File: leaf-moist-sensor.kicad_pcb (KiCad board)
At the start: 2 copper layers, 61 x 61 mm, 2 parts, among them P1 CONN_01X02

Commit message: 1mm Clearance + gerbers
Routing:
- net /SENSOR_TRACK: track 733.1 -> 690.1 mm
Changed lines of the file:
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@@
   )
   (setup
-    (last_trace_width 0.7)
+    (last_trace_width 0.25)
     (user_trace_width 0.7)
     (trace_clearance 0.2)
-    (zone_clearance 0.508)
+    (zone_clearance 1)
     (zone_45_only no)
     (trace_min 0.2)
@@
       (drillshape 0)
       (scaleselection 1)
-      (outputdirectory "05mmGerbers"))
+      (outputdirectory "1mmGerbers"))
   )
   (net 0 "")
@@
   (segment (start 132.85 60.1) (end 132.55 60.4) (width 0.7) (layer F.Cu) (net 1))
   (segment (start 132.85 57.85) (end 132.85 60.1) (width 0.7) (layer F.Cu) (net 1))
-  (segment (start 134.05 62.5) (end 134.05 114.6) (width 0.7) (layer F.Cu) (net 2))
-  (segment (start 134.1 62.8) (end 149.323337 62.8) (width 0.7) (layer F.Cu) (net 2))
-  (segment (start 134.1 66.3) (end 153.695918 66.3) (width 0.7) (layer F.Cu) (net 2))
-  (segment (start 134.1 69.8) (end 156.721892 69.8) (width 0.7) (layer F.Cu) (net 2))
-  (segment (start 134.1 73.3) (end 158.899194 73.3) (width 0.7) (layer F.Cu) (net 2))
-  (segment (start 134.1 76.8) (end 160.439134 76.8) (width 0.7) (layer F.Cu) (net 2))
-  (segment (start 134.1 80.3) (end 161.449589 80.3) (width 0.7) (layer F.Cu) (net 2))
-  (segment (start 134.1 83.8) (end 161.98817 83.8) (width 0.7) (layer F.Cu) (net 2))
-  (segment (start 134.1 87.3) (end 162.082137 87.3) (width 0.7) (layer F.Cu) (net 2))
-  (segment (start 134.1 90.8) (end 161.736027 90.8) (width 0.7) (layer F.Cu) (net 2))
-  (segment (start 134.1 94.3) (end 160.932816 94.3) (width 0.7) (layer F.Cu) (net 2))
-  (segment (start 134.1 97.8) (end 159.629395 97.8) (width 0.7) (layer F.Cu) (net 2))
-  (segment (start 134.1 101.3) (end 157.743181 101.3) (width 0.7) (layer F.Cu) (net 2))
-  (segment (start 134.1 104.8) (end 155.11785 104.8) (width 0.7) (layer F.Cu) (net 2))
-  (segment (start 134.1 108.3) (end 151.420508 108.3) (width 0.7) (layer F.Cu) (net 2))
-  (segment (start 134.1 111.8) (end 145.665034 111.8) (width 0.7) (layer F.Cu) (net 2))
-  (segment (start 134.05 64.55) (end 116.41658 64.55) (width 0.7) (layer F.Cu) (net 2))
-  (segment (start 134.05 68.05) (end 112.814711 68.05) (width 0.7) (layer F.Cu) (net 2))
-  (segment (start 134.05 71.55) (end 110.250053 71.55) (width 0.7) (layer F.Cu) (net 2))
-  (segment (start 134.05 75.05) (end 108.409456 75.05) (width 0.7) (layer F.Cu) (net 2))
-  (segment (start 134.05 78.55) (end 107.143913 78.55) (width 0.7) (layer F.Cu) (net 2))
-  (segment (start 134.05 82.05) (end 106.374424 82.05) (width 0.7) (layer F.Cu) (net 2))
-  (segment (start 134.05 85.55) (end 106.060046 85.55) (width 0.7) (layer F.Cu) (net 2))
-  (segment (start 134.05 89.05) (end 106.185372 89.05) (width 0.7) (layer F.Cu) (net 2))
-  (segment (start 134.05 92.55) (end 106.756457 92.55) (width 0.7) (layer F.Cu) (net 2))
-  (segment (start 134.05 96.05) (end 107.802381 96.05) (width 0.7) (layer F.Cu) (net 2))
-  (segment (start 134.05 99.55) (end 109.383474 99.55) (width 0.7) (layer F.Cu) (net 2))
-  (segment (start 134.05 103.05) (end 111.612587 103.05) (width 0.7) (layer F.Cu) (net 2))
-  (segment (start 134.05 106.55) (end 114.712536 106.55) (width 0.7) (layer F.Cu) (net 2))
-  (segment (start 134.05 110.05) (end 119.21971 110.05) (width 0.7) (layer F.Cu) (net 2))
+  (segment (start 134.05 62.5) (end 134.05 113.5) (width 0.7) (layer F.Cu) (net 2))
+  (segment (start 134.1 62.8) (end 148.152824 62.8) (width 0.7) (layer F.Cu) (net 2))
+  (segment (start 134.1 66.3) (end 152.3679 66.3) (width 0.7) (layer F.Cu) (net 2))
+  (segment (start 134.1 69.8) (end 155.295018 69.8) (width 0.7) (layer F.Cu) (net 2))
+  (segment (start 134.1 73.3) (end 157.40523 73.3) (width 0.7) (layer F.Cu) (net 2))
+  (segment (start 134.1 76.8) (end 158.899484 76.8) (width 0.7) (layer F.Cu) (net 2))
+  (segment (start 134.1 80.3) (end 159.880684 80.3) (width 0.7) (layer F.Cu) (net 2))
+  (segment (start 134.1 83.8) (end 160.403892 83.8) (width 0.7) (layer F.Cu) (net 2))
+  (segment (start 134.1 87.3) (end 160.495193 87.3) (width 0.7) (layer F.Cu) (net 2))
+  (segment (start 134.1 90.8) (end 160.158928 90.8) (width 0.7) (layer F.Cu) (net 2))
+  (segment (start 134.1 94.3) (end 159.378804 94.3) (width 0.7) (layer F.Cu) (net 2))
+  (segment (start 134.1 97.8) (end 158.113596 97.8) (width 0.7) (layer F.Cu) (net 2))
+  (segment (start 134.1 101.3) (end 156.284453 101.3) (width 0.7) (layer F.Cu) (net 2))
+  (segment (start 134.1 104.8) (end 153.742493 104.8) (width 0.7) (layer F.Cu) (net 2))
+  (segment (start 134.1 108.3) (end 150.171971 108.3) (width 0.7) (layer F.Cu) (net 2))
+  (segment (start 134.1 111.8) (end 144.644811 111.8) (width 0.7) (layer F.Cu) (net 2))
+  (segment (start 134.05 64.55) (end 117.676345 64.55) (width 0.7) (layer F.Cu) (net 2))
+  (segment (start 134.05 68.05) (end 114.197164 68.05) (width 0.7) (layer F.Cu) (net 2))
+  (segment (start 134.05 71.55) (end 111.713608 71.55) (width 0.7) (layer F.Cu) (net 2))
+  (segment (start 134.05 75.05) (end 109.928551 75.05) (width 0.7) (layer F.Cu) (net 2))
+  (segment (start 134.05 78.55) (end 108.700046 78.55) (width 0.7) (layer F.Cu) (net 2))
+  (segment (start 134.05 82.05) (end 107.952652 82.05) (width 0.7) (layer F.Cu) (net 2))
+  (segment (start 134.05 85.55) (end 107.647212 85.55) (width 0.7) (layer F.Cu) (net 2))
+  (segment (start 134.05 89.05) (end 107.768981 89.05) (width 0.7) (layer F.Cu) (net 2))
+  (segment (start 134.05 92.55) (end 108.323753 92.55) (width 0.7) (layer F.Cu) (net 2))
+  (segment (start 134.05 96.05) (end 109.339354 96.05) (width 0.7) (layer F.Cu) (net 2))
+  (segment (start 134.05 99.55) (end 110.873436 99.55) (width 0.7) (layer F.Cu) (net 2))
+  (segment (start 134.05 103.05) (end 113.033631 103.05) (width 0.7) (layer F.Cu) (net 2))
+  (segment (start 134.05 106.55) (end 116.031768 106.55) (width 0.7) (layer F.Cu) (net 2))
+  (segment (start 134.05 110.05) (end 120.375014 110.05) (width 0.7) (layer F.Cu) (net 2))
   (segment (start 134.05 60.4) (end 134.05 62.5) (width 0.7) (layer F.Cu) (net 2))
   (segment (start 136.239999 58.699999) (end 136.249999 58.699999) (width 0.7) (layer F.Cu) (net 3))
@@
   (segment (start 136.249999 58.699999) (end 136.7 59.15) (width 0.7) (layer F.Cu) (net 3))
   (zone (net 3) (net_name GND) (layer F.Cu) (hatch edge 0.508)
-    (connect_pads (clearance 0.508))
+    (connect_pads (clearance 1))
     (min_thickness 0.254)
     (fill yes (arc_segments 16) (thermal_gap 0.508) (thermal_bridge_width 0.508))

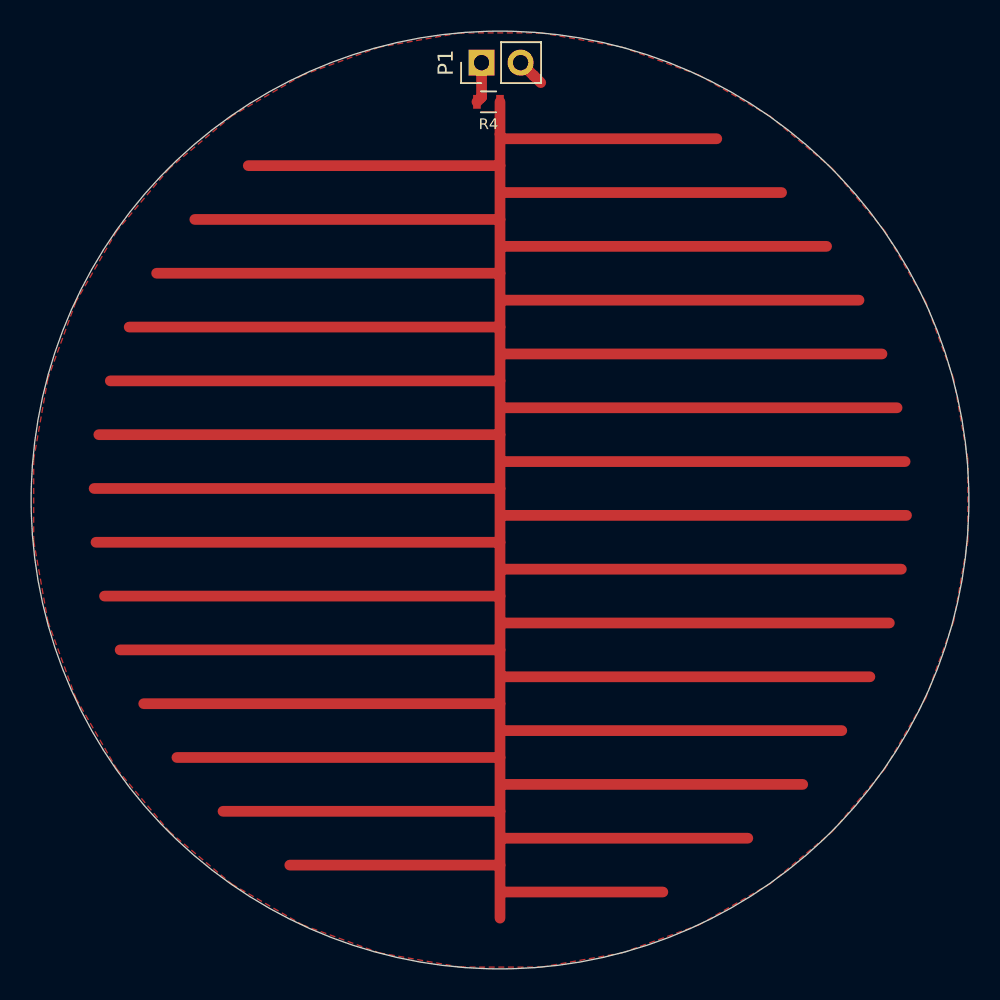
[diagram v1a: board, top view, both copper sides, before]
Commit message: 9 tracks, 1.5mm clearance
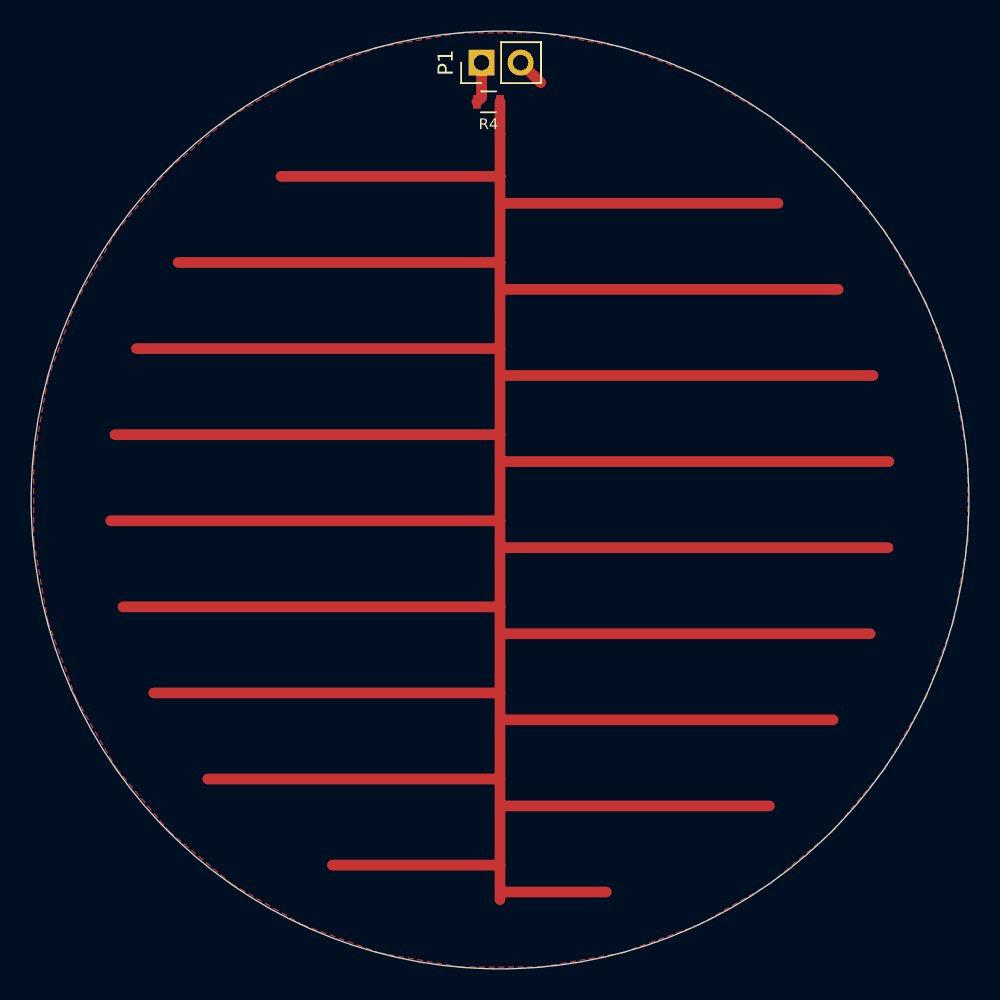
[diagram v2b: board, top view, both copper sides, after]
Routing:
- net /SENSOR_TRACK: track 690.1 -> 422.7 mm
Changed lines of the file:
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@@
     (thickness 1.6)
     (drawings 1)
-    (tracks 37)
+    (tracks 27)
     (zones 0)
     (modules 2)
@@
     (user_trace_width 0.7)
     (trace_clearance 0.2)
-    (zone_clearance 1)
+    (zone_clearance 1.5)
     (zone_45_only no)
     (trace_min 0.2)
@@
   (segment (start 132.85 60.1) (end 132.55 60.4) (width 0.7) (layer F.Cu) (net 1))
   (segment (start 132.85 57.85) (end 132.85 60.1) (width 0.7) (layer F.Cu) (net 1))
-  (segment (start 134.05 62.5) (end 134.05 113.5) (width 0.7) (layer F.Cu) (net 2))
-  (segment (start 134.1 62.8) (end 148.152824 62.8) (width 0.7) (layer F.Cu) (net 2))
-  (segment (start 134.1 66.3) (end 152.3679 66.3) (width 0.7) (layer F.Cu) (net 2))
-  (segment (start 134.1 69.8) (end 155.295018 69.8) (width 0.7) (layer F.Cu) (net 2))
-  (segment (start 134.1 73.3) (end 157.40523 73.3) (width 0.7) (layer F.Cu) (net 2))
-  (segment (start 134.1 76.8) (end 158.899484 76.8) (width 0.7) (layer F.Cu) (net 2))
-  (segment (start 134.1 80.3) (end 159.880684 80.3) (width 0.7) (layer F.Cu) (net 2))
-  (segment (start 134.1 83.8) (end 160.403892 83.8) (width 0.7) (layer F.Cu) (net 2))
-  (segment (start 134.1 87.3) (end 160.495193 87.3) (width 0.7) (layer F.Cu) (net 2))
-  (segment (start 134.1 90.8) (end 160.158928 90.8) (width 0.7) (layer F.Cu) (net 2))
-  (segment (start 134.1 94.3) (end 159.378804 94.3) (width 0.7) (layer F.Cu) (net 2))
-  (segment (start 134.1 97.8) (end 158.113596 97.8) (width 0.7) (layer F.Cu) (net 2))
-  (segment (start 134.1 101.3) (end 156.284453 101.3) (width 0.7) (layer F.Cu) (net 2))
-  (segment (start 134.1 104.8) (end 153.742493 104.8) (width 0.7) (layer F.Cu) (net 2))
-  (segment (start 134.1 108.3) (end 150.171971 108.3) (width 0.7) (layer F.Cu) (net 2))
-  (segment (start 134.1 111.8) (end 144.644811 111.8) (width 0.7) (layer F.Cu) (net 2))
-  (segment (start 134.05 64.55) (end 117.676345 64.55) (width 0.7) (layer F.Cu) (net 2))
-  (segment (start 134.05 68.05) (end 114.197164 68.05) (width 0.7) (layer F.Cu) (net 2))
-  (segment (start 134.05 71.55) (end 111.713608 71.55) (width 0.7) (layer F.Cu) (net 2))
-  (segment (start 134.05 75.05) (end 109.928551 75.05) (width 0.7) (layer F.Cu) (net 2))
-  (segment (start 134.05 78.55) (end 108.700046 78.55) (width 0.7) (layer F.Cu) (net 2))
-  (segment (start 134.05 82.05) (end 107.952652 82.05) (width 0.7) (layer F.Cu) (net 2))
-  (segment (start 134.05 85.55) (end 107.647212 85.55) (width 0.7) (layer F.Cu) (net 2))
-  (segment (start 134.05 89.05) (end 107.768981 89.05) (width 0.7) (layer F.Cu) (net 2))
-  (segment (start 134.05 92.55) (end 108.323753 92.55) (width 0.7) (layer F.Cu) (net 2))
-  (segment (start 134.05 96.05) (end 109.339354 96.05) (width 0.7) (layer F.Cu) (net 2))
-  (segment (start 134.05 99.55) (end 110.873436 99.55) (width 0.7) (layer F.Cu) (net 2))
-  (segment (start 134.05 103.05) (end 113.033631 103.05) (width 0.7) (layer F.Cu) (net 2))
-  (segment (start 134.05 106.55) (end 116.031768 106.55) (width 0.7) (layer F.Cu) (net 2))
-  (segment (start 134.05 110.05) (end 120.375014 110.05) (width 0.7) (layer F.Cu) (net 2))
+  (segment (start 134.1 67) (end 152.133726 67) (width 0.7) (layer F.Cu) (net 2))
+  (segment (start 134.1 72.6) (end 156.048657 72.6) (width 0.7) (layer F.Cu) (net 2))
+  (segment (start 134.1 78.2) (end 158.314227 78.2) (width 0.7) (layer F.Cu) (net 2))
+  (segment (start 134.1 83.8) (end 159.347707 83.8) (width 0.7) (layer F.Cu) (net 2))
+  (segment (start 134.1 89.4) (end 159.290258 89.4) (width 0.7) (layer F.Cu) (net 2))
+  (segment (start 134.1 95) (end 158.134652 95) (width 0.7) (layer F.Cu) (net 2))
+  (segment (start 134.1 100.6) (end 155.719801 100.6) (width 0.7) (layer F.Cu) (net 2))
+  (segment (start 134.1 106.2) (end 151.578371 106.2) (width 0.7) (layer F.Cu) (net 2))
+  (segment (start 134.1 111.8) (end 140.964663 111.8) (width 0.7) (layer F.Cu) (net 2))
+  (segment (start 134.05 70.85) (end 113.114569 70.85) (width 0.7) (layer F.Cu) (net 2))
+  (segment (start 134.05 76.45) (end 110.399542 76.45) (width 0.7) (layer F.Cu) (net 2))
+  (segment (start 134.05 82.05) (end 109.004803 82.05) (width 0.7) (layer F.Cu) (net 2))
+  (segment (start 134.05 87.65) (end 108.726776 87.65) (width 0.7) (layer F.Cu) (net 2))
+  (segment (start 134.05 93.25) (end 109.530279 93.25) (width 0.7) (layer F.Cu) (net 2))
+  (segment (start 134.05 98.85) (end 111.521564 98.85) (width 0.7) (layer F.Cu) (net 2))
+  (segment (start 134.05 104.45) (end 115.037901 104.45) (width 0.7) (layer F.Cu) (net 2))
+  (segment (start 134.05 110.05) (end 123.145216 110.05) (width 0.7) (layer F.Cu) (net 2))
   (segment (start 134.05 60.4) (end 134.05 62.5) (width 0.7) (layer F.Cu) (net 2))
+  (segment (start 134.05 65.25) (end 119.8 65.25) (width 0.7) (layer F.Cu) (net 2))
+  (segment (start 134.05 62.5) (end 134.05 65.25) (width 0.7) (layer F.Cu) (net 2))
+  (segment (start 134.05 65.25) (end 134.05 112.3) (width 0.7) (layer F.Cu) (net 2))
   (segment (start 136.239999 58.699999) (end 136.249999 58.699999) (width 0.7) (layer F.Cu) (net 3))
   (segment (start 135.39 57.85) (end 136.239999 58.699999) (width 0.7) (layer F.Cu) (net 3))
   (segment (start 136.249999 58.699999) (end 136.7 59.15) (width 0.7) (layer F.Cu) (net 3))
   (zone (net 3) (net_name GND) (layer F.Cu) (hatch edge 0.508)
-    (connect_pads (clearance 1))
+    (connect_pads (clearance 1.5))
     (min_thickness 0.254)
     (fill yes (arc_segments 16) (thermal_gap 0.508) (thermal_bridge_width 0.508))
